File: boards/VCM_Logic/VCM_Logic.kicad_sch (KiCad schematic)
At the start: 0 parts

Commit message: Added NUCLEO144-F767ZI symbol
Add the NUCLEO144-F767ZI MCU module symbol to the schematic.

Now waiting on further specs/reqs for the project.
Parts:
- added U1: NUCLEO144-F767ZI, Module:ST_Morpho_Connector_144_STLink, symbol MCU_Module:NUCLEO144-F767ZI

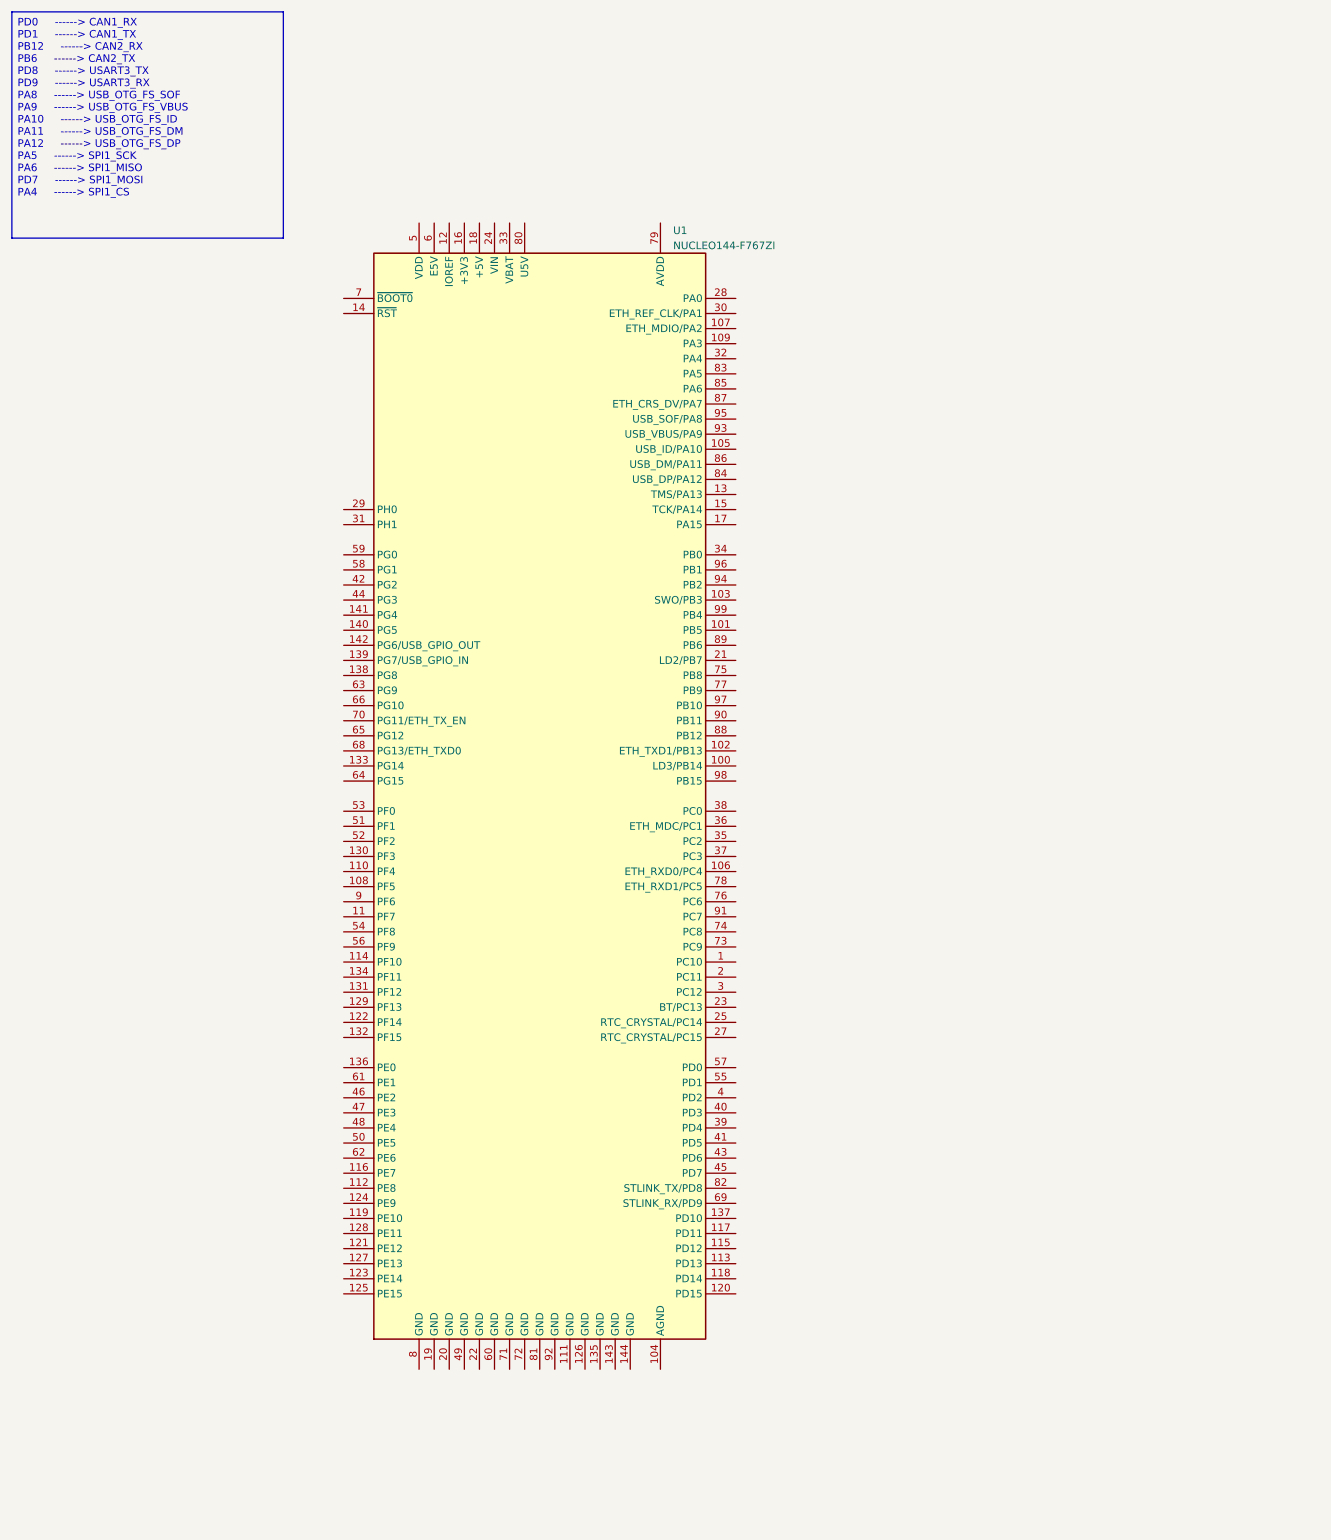
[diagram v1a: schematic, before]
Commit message: Updated STM chip to have proper footprint.
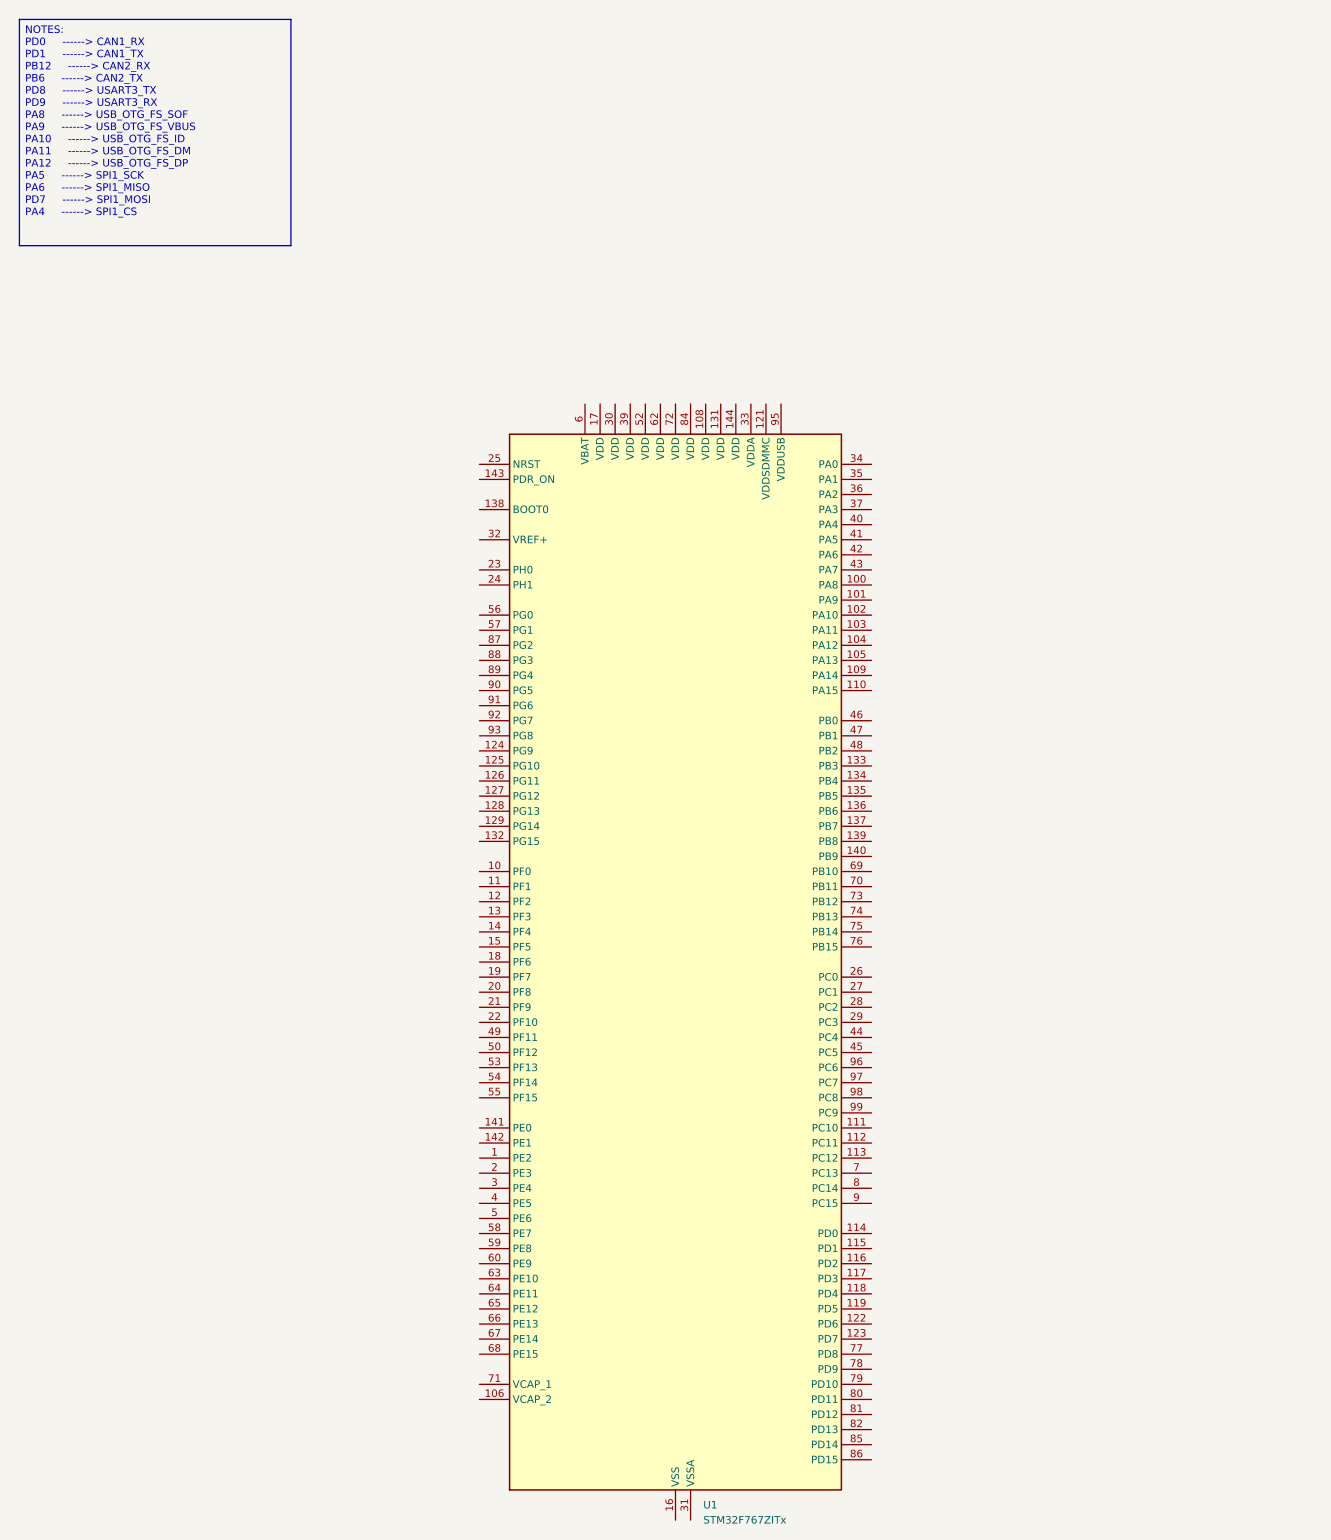
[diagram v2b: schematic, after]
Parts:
- removed U1: NUCLEO144-F767ZI, Module:ST_Morpho_Connector_144_STLink, symbol MCU_Module:NUCLEO144-F767ZI
- added U1: STM32F767ZITx, Package_QFP:LQFP-144_20x20mm_P0.5mm, symbol MCU_ST_STM32F7:STM32F767ZITx
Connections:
- new net: U1.107 (VSS), U1.120 (VSS), U1.130 (VSS), U1.16 (VSS), U1.38 (VSS), U1.51 (VSS), U1.61 (VSS), U1.83 (VSS), U1.94 (VSS)

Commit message: Started putting together basic stuff
Added some hierarchal sheets to the document. Begun adding basic things to the MCU sheet.
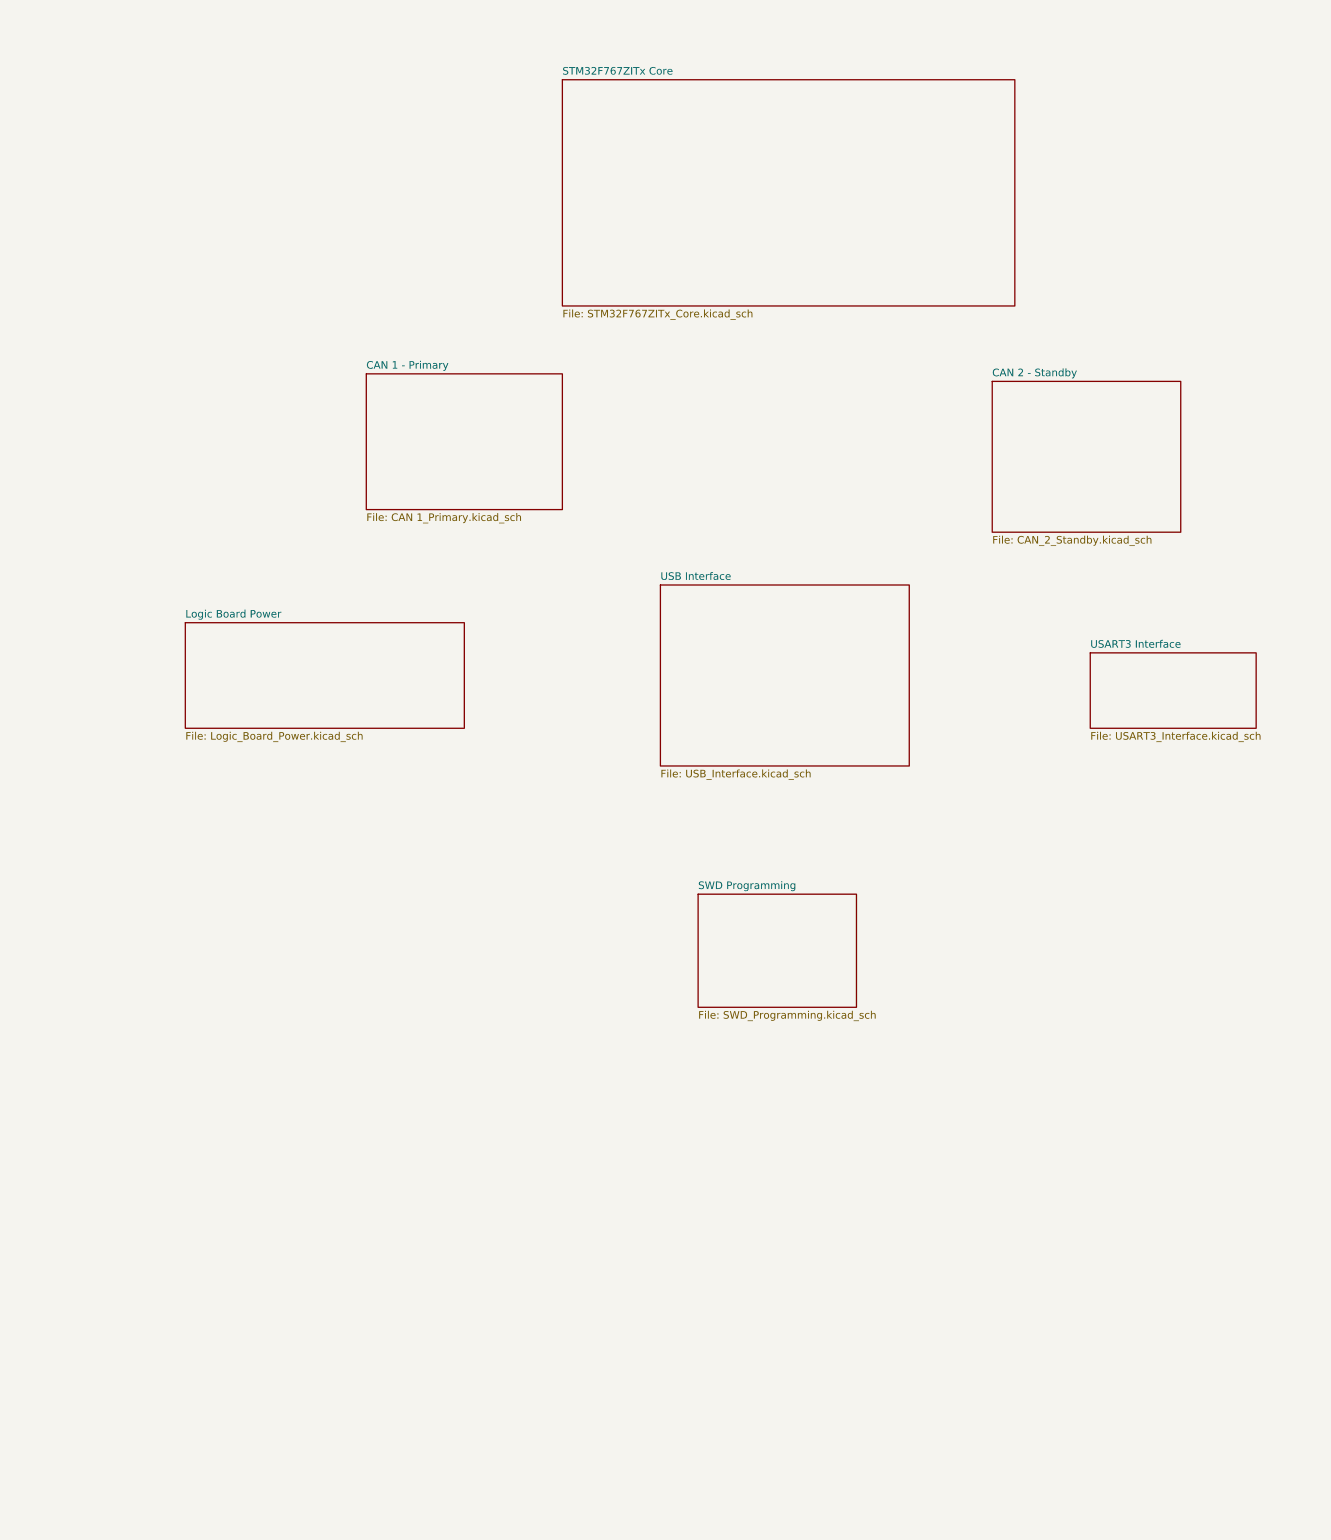
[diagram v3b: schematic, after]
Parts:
- removed U1: STM32F767ZITx, Package_QFP:LQFP-144_20x20mm_P0.5mm, symbol MCU_ST_STM32F7:STM32F767ZITx
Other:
- added sheet CAN 1 - Primary (CAN 1_Primary.kicad_sch)
- added sheet CAN 2 - Standby (CAN_2_Standby.kicad_sch)
- added sheet Logic Board Power (Logic_Board_Power.kicad_sch)
- added sheet STM32F767ZITx Core (STM32F767ZITx_Core.kicad_sch)
- added sheet SWD Programming (SWD_Programming.kicad_sch)
- added sheet USART3 Interface (USART3_Interface.kicad_sch)
- added sheet USB Interface (USB_Interface.kicad_sch)
